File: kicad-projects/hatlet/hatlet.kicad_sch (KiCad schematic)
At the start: 51 parts, among them J1 Racklet_USBHeader_02x06, J2 SWD, J3 PMOD0, J4 PMOD2, J5 PMOD1, J6 UART0, J7 PMOD3, SW1 BOOTSEL, SW2 RESET, U1 AMS1117-3.3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

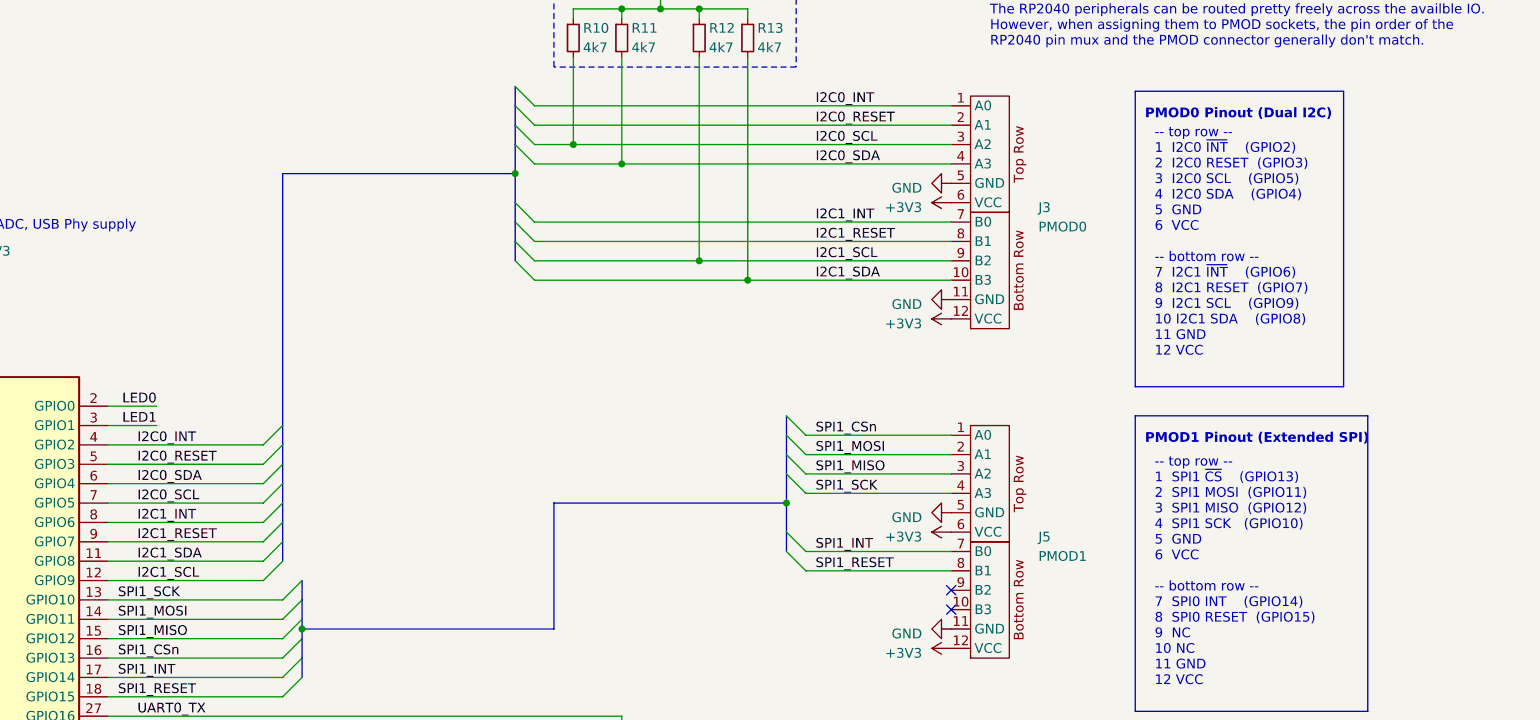
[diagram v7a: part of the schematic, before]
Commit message: hatlet: Fix PMOD0 I2C1 pinout
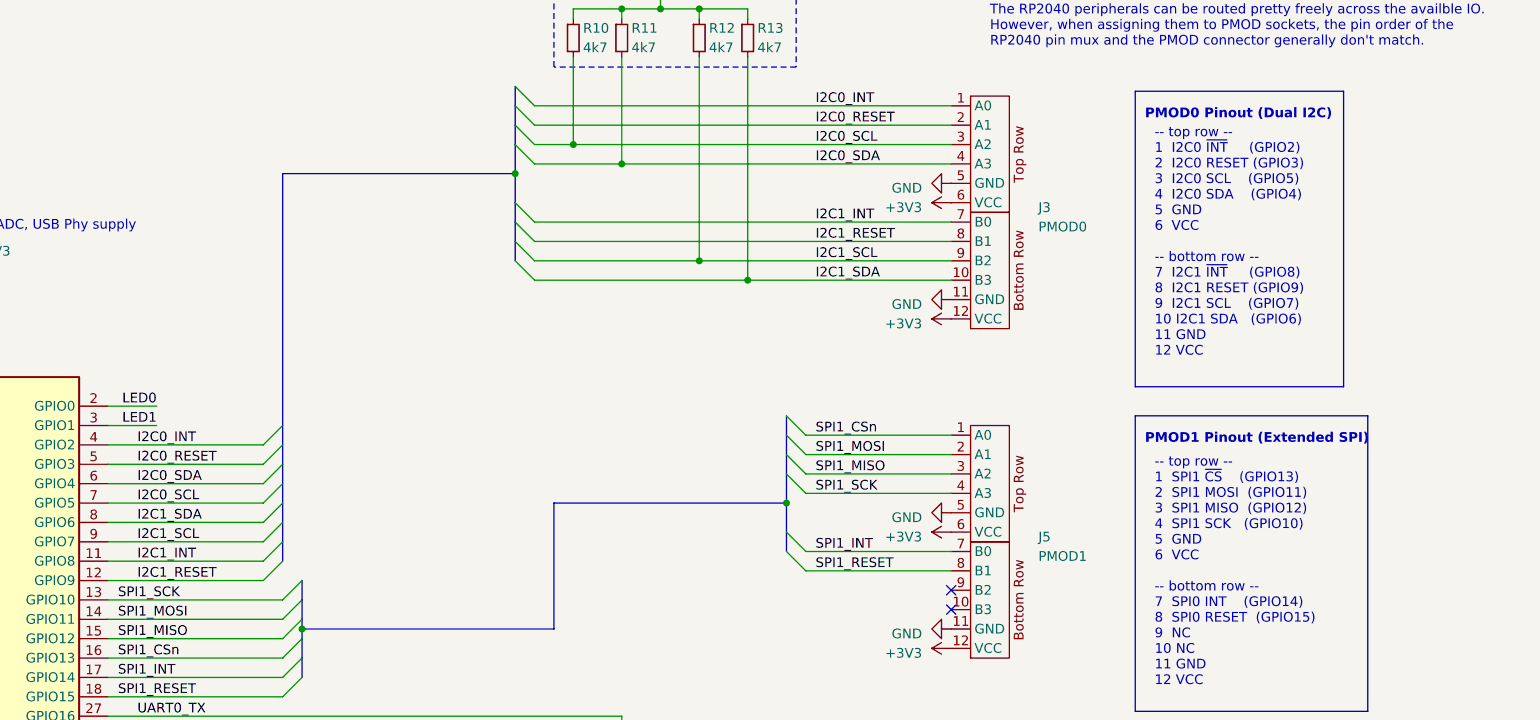
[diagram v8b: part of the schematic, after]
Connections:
- net I2C1_INT: now also U2.11 (GPIO8); no longer U2.8 (GPIO6)
- net I2C1_RESET: now also U2.12 (GPIO9); no longer U2.9 (GPIO7)
- net I2C1_SCL: now also U2.9 (GPIO7); no longer U2.12 (GPIO9)
- net I2C1_SDA: now also U2.8 (GPIO6); no longer U2.11 (GPIO8)
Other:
- note added: "-- top row -- 1 I2C0 ~{INT} (GPIO2) 2 I2C0 RESET (GPIO3) 3 I2C0 SCL (GPIO5) 4 I2C0 SDA (GPIO4) 5 GND 6 VCC -- bottom row -- 7 I2C1 ~{INT} (GPIO8) 8 I2C1 RESET (GPIO9) 9 I2C1 SCL (GPIO7) 10 I2C1 SDA (GPIO6) 11 GND 12 VCC"
- note removed: "-- top row -- 1 I2C0 ~{INT} (GPIO2) 2 I2C0 RESET (GPIO3) 3 I2C0 SCL (GPIO5) 4 I2C0 SDA (GPIO4) 5 GND 6 VCC -- bottom row -- 7 I2C1 ~{INT} (GPIO6) 8 I2C1 RESET (GPIO7) 9 I2C1 SCL (GPIO9) 10 I2C1 SDA (GPIO8) 11 GND 12 VCC"
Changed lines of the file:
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@@
     (effects (font (size 1.27 1.27) (thickness 0.254) bold) (justify left bottom))
   )
-  (text "-- top row --\n1  I2C0 ~{INT}    (GPIO2)\n2  I2C0 RESET  (GPIO3)\n3  I2C0 SCL    (GPIO5)\n4  I2C0 SDA    (GPIO4)\n5  GND\n6  VCC\n\n-- bottom row --\n7  I2C1 ~{INT}    (GPIO6)\n8  I2C1 RESET  (GPIO7)\n9  I2C1 SCL    (GPIO9)\n10 I2C1 SDA    (GPIO8)\n11 GND\n12 VCC"
+  (text "-- top row --\n1  I2C0 ~{INT}     (GPIO2)\n2  I2C0 RESET (GPIO3)\n3  I2C0 SCL    (GPIO5)\n4  I2C0 SDA    (GPIO4)\n5  GND\n6  VCC\n\n-- bottom row --\n7  I2C1 ~{INT}     (GPIO8)\n8  I2C1 RESET (GPIO9)\n9  I2C1 SCL    (GPIO7)\n10 I2C1 SDA   (GPIO6)\n11 GND\n12 VCC"
     (at 349.25 69.85 0)
     (effects (font (size 1.27 1.27)) (justify left bottom))
@@
     (effects (font (size 1.27 1.27)) (justify left bottom))
   )
-  (label "I2C1_RESET" (at 215.9 93.98 0) (fields_autoplaced)
+  (label "I2C1_RESET" (at 215.9 99.06 0) (fields_autoplaced)
     (effects (font (size 1.27 1.27)) (justify left bottom))
   )
@@
     (effects (font (size 1.27 1.27)) (justify right bottom))
   )
-  (label "I2C1_INT" (at 215.9 91.44 0) (fields_autoplaced)
-    (effects (font (size 1.27 1.27)) (justify left bottom))
-  )
-  (label "I2C1_SCL" (at 215.9 99.06 0) (fields_autoplaced)
+  (label "I2C1_INT" (at 215.9 96.52 0) (fields_autoplaced)
+    (effects (font (size 1.27 1.27)) (justify left bottom))
+  )
+  (label "I2C1_SCL" (at 215.9 93.98 0) (fields_autoplaced)
     (effects (font (size 1.27 1.27)) (justify left bottom))
   )
@@
     (effects (font (size 1.27 1.27)) (justify left bottom))
   )
-  (label "I2C1_SDA" (at 215.9 96.52 0) (fields_autoplaced)
-    (effects (font (size 1.27 1.27)) (justify left bottom))
-  )
+  (label "I2C1_SDA" (at 215.9 91.44 0) (fields_autoplaced)
+    (effects (font (size 1.27 1.27)) (justify left bottom))
+  )
